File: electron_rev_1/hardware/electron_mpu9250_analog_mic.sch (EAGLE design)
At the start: 33 parts, among them IC2 S25FL128SAGNFI011, IC4 MIC_I2S_SPH0645, U1 MPU-9250, U2 Value, U3 OPA322AIDBVT

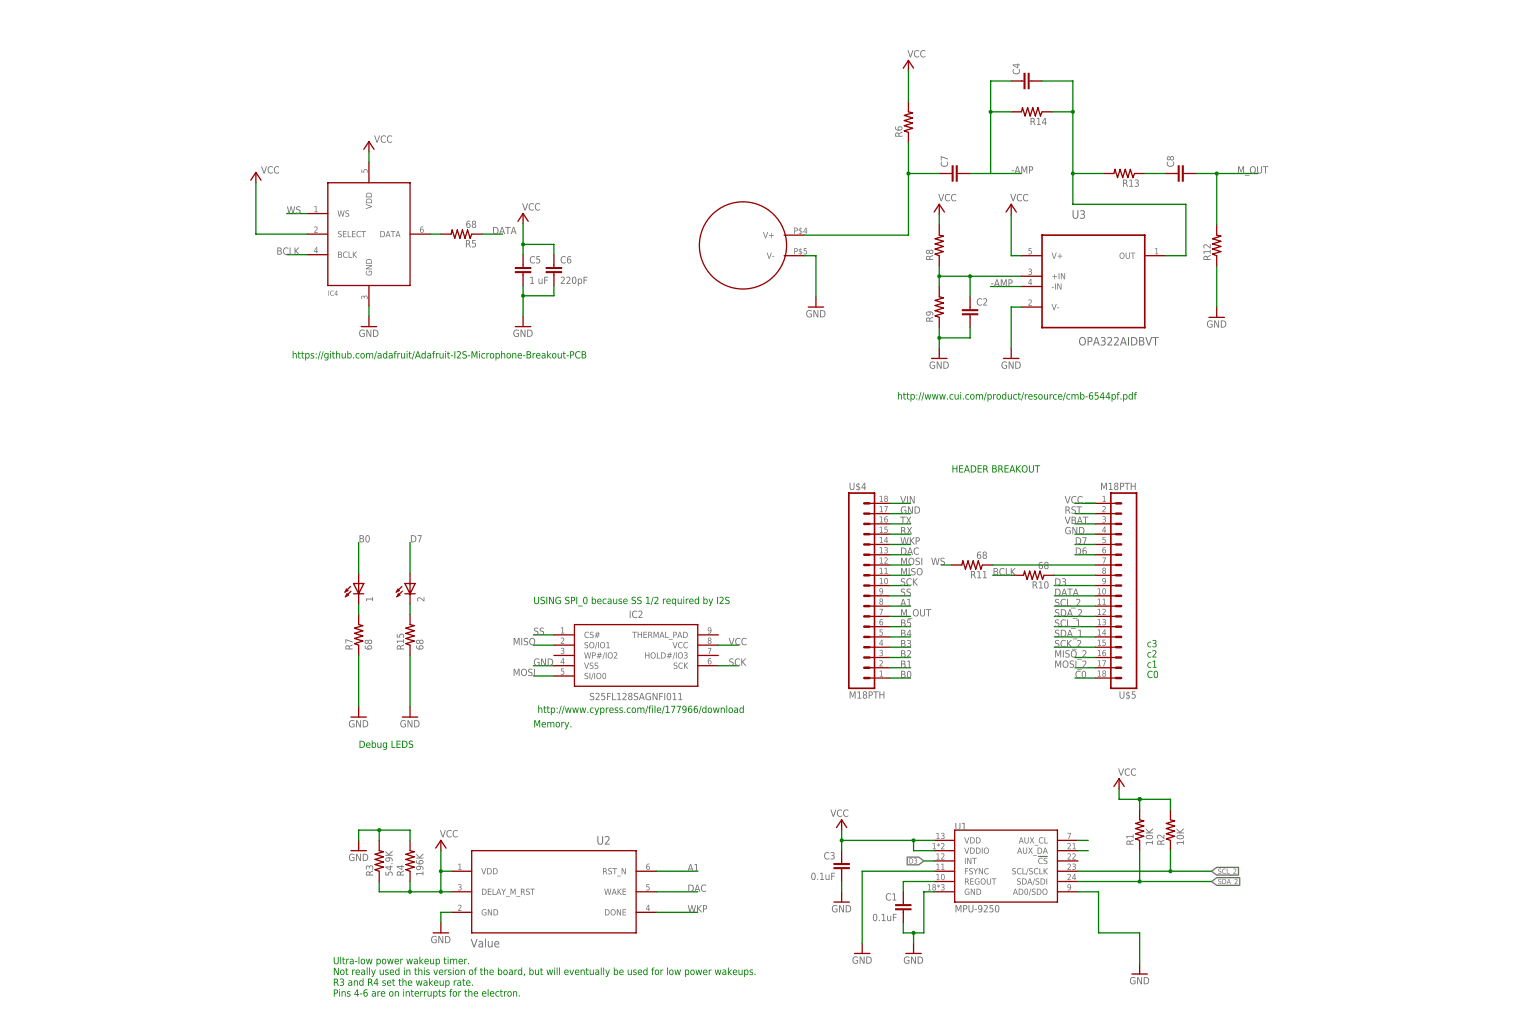
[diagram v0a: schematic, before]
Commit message: fixed grid issue in schematic. added sd card. added incomplete gas sensors
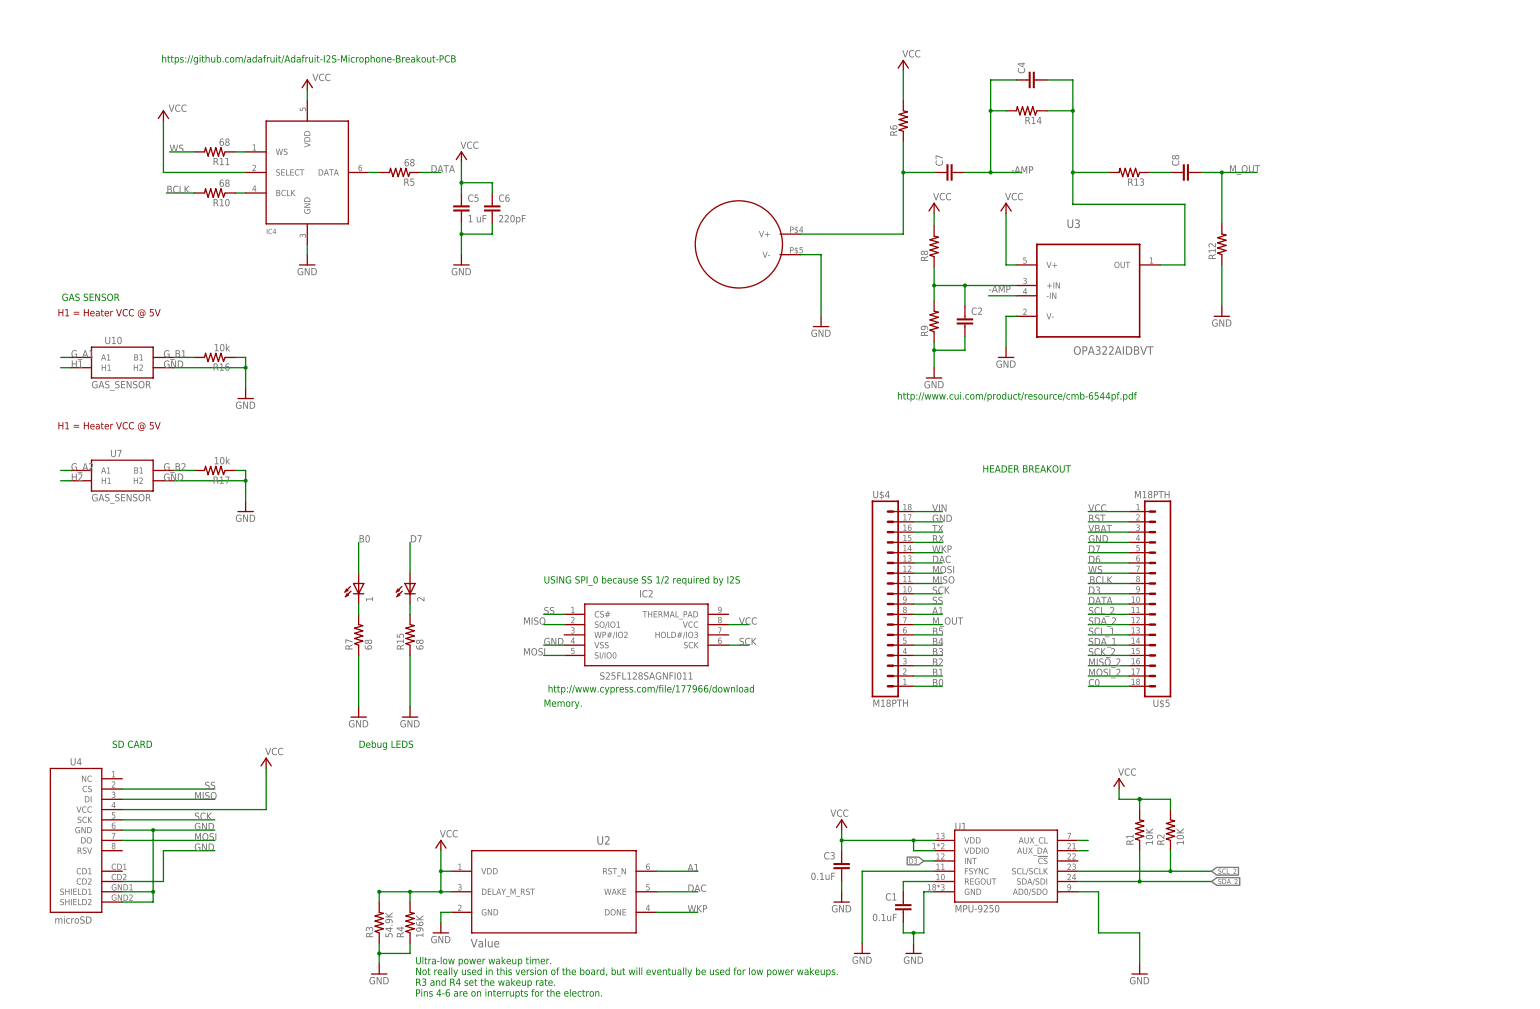
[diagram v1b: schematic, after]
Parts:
- added R16, R17: 10k, resistor:R-US_R0603
- added U10, U7: GAS_SENSOR, SparkFun:GAS_SENSOR
- added U4: microSD, SparkFun:USD-SOCKETSMD
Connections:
- new net G_A1: U10.A1
- new net G_A2: U7.A1
- new net G_B1: R16.2, U10.B1
- new net G_B2: R17.2, U7.B1
- new net H1: U10.H1
- new net H2: U7.H1
- net BCLK: now also U$5.8; no longer IC4.BCLK
- net GND: now also R16.1, R17.1, R3.1, R4.1, U10.H2, U4.CD2, U4.GND, U4.SHIELD1, U4.SHIELD2, U7.H2; no longer R3.2, R4.2
- net MISO: now also U4.DI
- net MOSI: now also U4.DO
- net N$2: now also IC4.WS, R11.1; no longer R10.1, U$5.8
- net N$4: now also IC4.BCLK, R10.1; no longer R11.1, U$5.7
- net SCK: now also U4.SCK
- net SS: now also U4.CS
- net VCC: now also R3.2, R4.2, U4.VCC; no longer R3.1, R4.1
- net WS: now also U$5.7; no longer IC4.WS
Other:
- note added: "GAS SENSOR"
- note added: "H1 = Heater VCC @ 5V"
- note added: "SD CARD"
- note removed: "C0"
- note removed: "c1"
- note removed: "c2"
- note removed: "c3"
- moved on the sheet: C2, C4, C5, C6, C7, C8, IC2, IC4, R10, R11, R12, R13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

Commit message: added in that good looking Cal logo... woooooo... also did a bit more wiring for the gas sensors
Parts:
- added L1: UCB_CAL100MIL, logos:UCB_CAL100MIL
- added SJ2: JUMPER_PAD-3-1&2_NC_BY_PASTE, SparkFun-Passives:JUMPER_PAD-3-1&2_NC_BY_PASTE
- added U5, U6: +12v, SparkFun-IC-Power:V_REG_78XX7812
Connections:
- new net N$10: SJ2.1, U5.IN, U6.IN
- net GND: now also SJ2.3, U5.GND, U6.GND
- net H1: now also U5.OUT
- net H2: now also U6.OUT
- net VCC: now also SJ2.2
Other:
- moved on the sheet: 1, 2, R15, R16, R17, R7, U10, U7

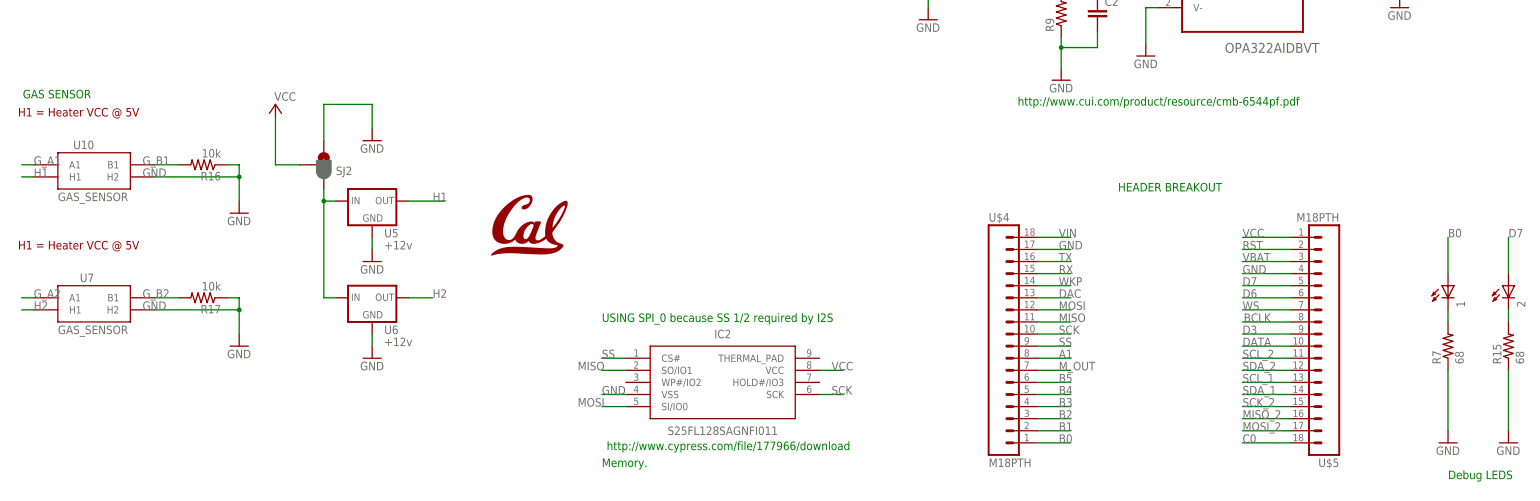
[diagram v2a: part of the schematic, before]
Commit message: generic gas sensors hooked up... haven't set up fancy CO relay thing yet. Don't know if it's worth it. Also last commit had gas sensors wired incorrectly
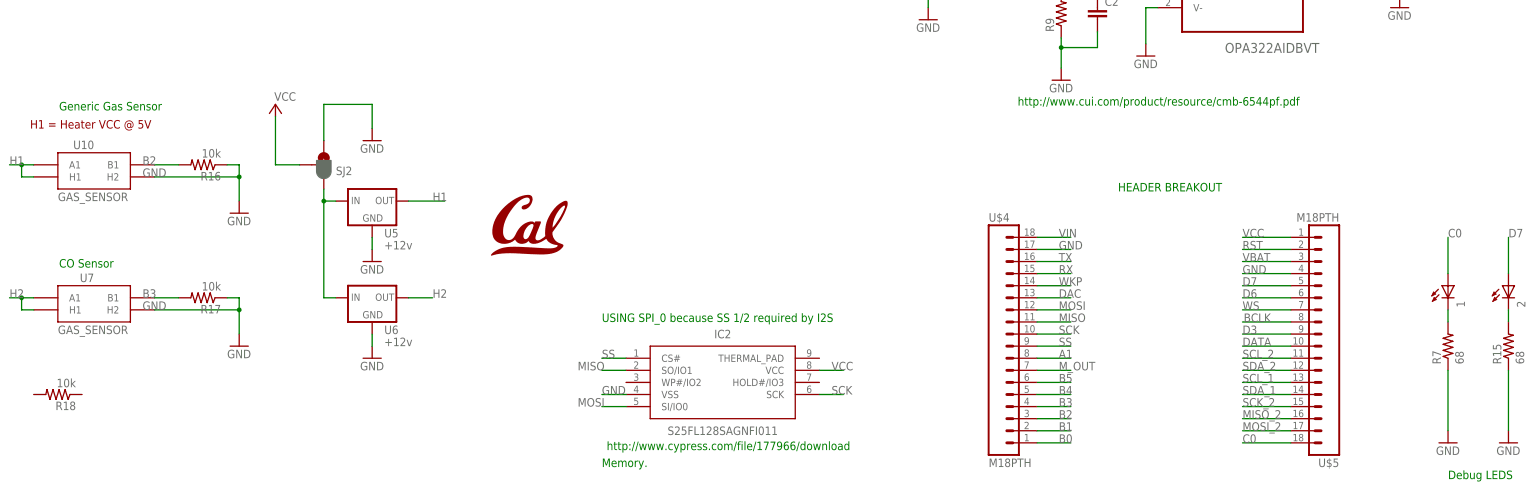
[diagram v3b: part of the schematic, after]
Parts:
- added R18: 10k, resistor:R-US_R0603
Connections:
- removed net G_A1: U10.A1
- removed net G_A2: U7.A1
- removed net G_B1: R16.2, U10.B1
- removed net G_B2: R17.2, U7.B1
- net B0: no longer 1.A
- net B2: now also R16.2, U10.B1
- net B3: now also R17.2, U7.B1
- net C0: now also 1.A
- net H1: now also U10.A1
- net H2: now also U7.A1
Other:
- note added: "CO Sensor"
- note added: "Generic Gas Sensor"
- note removed: "GAS SENSOR"
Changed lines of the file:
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@@
 <part name="GND19" library="supply1" library_urn="urn:adsk.eagle:library:371" deviceset="GND" device=""/>
 <part name="L1" library="logos" deviceset="UCB_CAL" device="100MIL"/>
+<part name="R18" library="resistor" library_urn="urn:adsk.eagle:library:348" deviceset="R-US_" device="R0603" package3d_urn="urn:adsk.eagle:package:26057/1" value="10k"/>
 </parts>
 <sheets>
@@
 <text x="33.02" y="45.72" size="1.778" layer="91">Memory. </text>
 <text x="141.478" y="103.632" size="1.778" layer="91">HEADER BREAKOUT</text>
-<text x="-88.646" y="123.19" size="1.778" layer="91">GAS SENSOR</text>
+<text x="-81.026" y="87.63" size="1.778" layer="91">CO Sensor</text>
 <text x="-73.66" y="35.56" size="1.778" layer="91">SD CARD</text>
 <text x="35.56" y="200.66" size="1.778" layer="91">SD CARD</text>
-<text x="-89.662" y="91.44" size="1.778" layer="94">H1 = Heater VCC @ 5V</text>
-<text x="-89.662" y="119.38" size="1.778" layer="94">H1 = Heater VCC @ 5V</text>
+<text x="-87.122" y="116.84" size="1.778" layer="94">H1 = Heater VCC @ 5V</text>
+<text x="-81.026" y="120.65" size="1.778" layer="91">Generic Gas Sensor</text>
 </plain>
 <instances>
@@
 <instance part="GND19" gate="1" x="-15.24" y="114.3"/>
 <instance part="L1" gate="G$1" x="17.78" y="96.52"/>
+<instance part="R18" gate="G$1" x="-81.28" y="60.96" rot="R180"/>
 </instances>
 <busses>
@@
 <label x="129.032" y="58.42" size="1.778" layer="95"/>
 </segment>
+<segment>
+<label x="-63.5" y="81.28" size="1.778" layer="95"/>
+<pinref part="U7" gate="G$1" pin="B1"/>
+<pinref part="R17" gate="G$1" pin="2"/>
+<wire x1="-60.96" y1="81.28" x2="-55.88" y2="81.28" width="0.1524" layer="91"/>
+</segment>
 </net>
 <net name="B2" class="0">
@@
 <label x="129.032" y="55.88" size="1.778" layer="95"/>
 </segment>
+<segment>
+<label x="-63.5" y="109.22" size="1.778" layer="95"/>
+<pinref part="U10" gate="G$1" pin="B1"/>
+<pinref part="R16" gate="G$1" pin="2"/>
+<wire x1="-60.96" y1="109.22" x2="-55.88" y2="109.22" width="0.1524" layer="91"/>
+</segment>
 </net>
 <net name="B1" class="0">
@@
 <label x="129.032" y="50.8" size="1.778" layer="95"/>
 </segment>
+</net>
+<net name="RST" class="0">
+<segment>
+<pinref part="U$5" gate="G$1" pin="2"/>
+<wire x1="177.8" y1="91.44" x2="167.64" y2="91.44" width="0.1524" layer="91"/>
+<label x="167.64" y="91.44" size="1.778" layer="95"/>
+</segment>
+</net>
+<net name="VBAT" class="0">
+<segment>
+<pinref part="U$5" gate="G$1" pin="3"/>
+<wire x1="177.8" y1="88.9" x2="167.64" y2="88.9" width="0.1524" layer="91"/>
+<label x="167.64" y="88.9" size="1.778" layer="95"/>
+</segment>
+</net>
+<net name="D7" class="0">
+<segment>
+<pinref part="U$5" gate="G$1" pin="5"/>
+<wire x1="177.8" y1="83.82" x2="167.64" y2="83.82" width="0.1524" layer="91"/>
+<label x="167.64" y="83.82" size="1.778" layer="95"/>
+</segment>
+<segment>
+<pinref part="2" gate="G$1" pin="A"/>
+<wire x1="223.52" y1="86.36" x2="223.52" y2="93.98" width="0.1524" layer="91"/>
+<label x="223.52" y="93.98" size="1.778" layer="95"/>
+</segment>
+</net>
+<net name="SS" class="0">
+<segment>
+<pinref part="IC2" gate="G$1" pin="CS#"/>
+<wire x1="38.1" y1="68.58" x2="33.02" y2="68.58" width="0.1524" layer="91"/>
+<label x="33.02" y="68.58" size="1.778" layer="95"/>
+</segment>
+<segment>
+<pinref part="U$4" gate="G$1" pin="9"/>
+<wire x1="124.46" y1="71.12" x2="131.572" y2="71.12" width="0.1524" layer="91"/>
+<label x="129.032" y="71.12" size="1.778" layer="95"/>
+</segment>
+<segment>
+<wire x1="-71.12" y1="25.4" x2="-48.26" y2="25.4" width="0.1524" layer="91"/>
+<pinref part="U4" gate="G$1" pin="CS"/>
+<label x="-50.8" y="25.4" size="1.778" layer="95"/>
+</segment>
+</net>
+<net name="MISO_2" class="0">
+<segment>
+<pinref part="U$5" gate="G$1" pin="16"/>
+<wire x1="177.8" y1="55.88" x2="167.64" y2="55.88" width="0.1524" layer="91"/>
+<label x="167.64" y="55.88" size="1.778" layer="95"/>
+</segment>
+</net>
+<net name="MOSI_2" class="0">
+<segment>
+<pinref part="U$5" gate="G$1" pin="17"/>
+<wire x1="177.8" y1="53.34" x2="167.64" y2="53.34" width="0.1524" layer="91"/>
+<label x="167.64" y="53.34" size="1.778" layer="95"/>
+</segment>
+</net>
+<net name="C0" class="0">
+<segment>
+<pinref part="U$5" gate="G$1" pin="18"/>
+<wire x1="177.8" y1="50.8" x2="167.64" y2="50.8" width="0.1524" layer="91"/>
+<label x="167.64" y="50.8" size="1.778" layer="95"/>
+</segment>
 <segment>
 <pinref part="1" gate="G$1" pin="A"/>
 <wire x1="210.82" y1="86.36" x2="210.82" y2="93.98" width="0.1524" layer="91"/>
 <label x="210.82" y="93.98" size="1.778" layer="95"/>
-</segment>
-</net>
-<net name="RST" class="0">
-<segment>
-<pinref part="U$5" gate="G$1" pin="2"/>
-<wire x1="177.8" y1="91.44" x2="167.64" y2="91.44" width="0.1524" layer="91"/>
-<label x="167.64" y="91.44" size="1.778" layer="95"/>
-</segment>
-</net>
-<net name="VBAT" class="0">
-<segment>
-<pinref part="U$5" gate="G$1" pin="3"/>
-<wire x1="177.8" y1="88.9" x2="167.64" y2="88.9" width="0.1524" layer="91"/>
-<label x="167.64" y="88.9" size="1.778" layer="95"/>
-</segment>
-</net>
-<net name="D7" class="0">
-<segment>
-<pinref part="U$5" gate="G$1" pin="5"/>
-<wire x1="177.8" y1="83.82" x2="167.64" y2="83.82" width="0.1524" layer="91"/>
-<label x="167.64" y="83.82" size="1.778" layer="95"/>
-</segment>
-<segment>
-<pinref part="2" gate="G$1" pin="A"/>
-<wire x1="223.52" y1="86.36" x2="223.52" y2="93.98" width="0.1524" layer="91"/>
-<label x="223.52" y="93.98" size="1.778" layer="95"/>
-</segment>
-</net>
-<net name="SS" class="0">
-<segment>
-<pinref part="IC2" gate="G$1" pin="CS#"/>
-<wire x1="38.1" y1="68.58" x2="33.02" y2="68.58" width="0.1524" layer="91"/>
-<label x="33.02" y="68.58" size="1.778" layer="95"/>
-</segment>
-<segment>
-<pinref part="U$4" gate="G$1" pin="9"/>
-<wire x1="124.46" y1="71.12" x2="131.572" y2="71.12" width="0.1524" layer="91"/>
-<label x="129.032" y="71.12" size="1.778" layer="95"/>
-</segment>
-<segment>
-<wire x1="-71.12" y1="25.4" x2="-48.26" y2="25.4" width="0.1524" layer="91"/>
-<pinref part="U4" gate="G$1" pin="CS"/>
-<label x="-50.8" y="25.4" size="1.778" layer="95"/>
-</segment>
-</net>
-<net name="MISO_2" class="0">
-<segment>
-<pinref part="U$5" gate="G$1" pin="16"/>
-<wire x1="177.8" y1="55.88" x2="167.64" y2="55.88" width="0.1524" layer="91"/>
-<label x="167.64" y="55.88" size="1.778" layer="95"/>
-</segment>
-</net>
-<net name="MOSI_2" class="0">
-<segment>
-<pinref part="U$5" gate="G$1" pin="17"/>
-<wire x1="177.8" y1="53.34" x2="167.64" y2="53.34" width="0.1524" layer="91"/>
-<label x="167.64" y="53.34" size="1.778" layer="95"/>
-</segment>
-</net>
-<net name="C0" class="0">
-<segment>
-<pinref part="U$5" gate="G$1" pin="18"/>
-<wire x1="177.8" y1="50.8" x2="167.64" y2="50.8" width="0.1524" layer="91"/>
-<label x="167.64" y="50.8" size="1.778" layer="95"/>
 </segment>
 </net>
@@
 <segment>
 <wire x1="-88.9" y1="106.68" x2="-86.36" y2="106.68" width="0.1524" layer="91"/>
-<label x="-86.36" y="106.68" size="1.778" layer="95"/>
 <pinref part="U10" gate="G$1" pin="H1"/>
+<wire x1="-88.9" y1="109.22" x2="-86.36" y2="109.22" width="0.1524" layer="91"/>
+<label x="-91.44" y="109.22" size="1.778" layer="95"/>
+<pinref part="U10" gate="G$1" pin="A1"/>
+<wire x1="-88.9" y1="106.68" x2="-88.9" y2="109.22" width="0.1524" layer="91"/>
+<wire x1="-88.9" y1="109.22" x2="-91.44" y2="109.22" width="0.1524" layer="91"/>
+<junction x="-88.9" y="109.22"/>
 </segment>
 <segment>
@@
 <segment>
 <wire x1="-88.9" y1="78.74" x2="-86.36" y2="78.74" width="0.1524" layer="91"/>
-<label x="-86.36" y="78.74" size="1.778" layer="95"/>
 <pinref part="U7" gate="G$1" pin="H1"/>
+<wire x1="-88.9" y1="81.28" x2="-86.36" y2="81.28" width="0.1524" layer="91"/>
+<label x="-91.44" y="81.28" size="1.778" layer="95"/>
+<pinref part="U7" gate="G$1" pin="A1"/>
+<wire x1="-88.9" y1="78.74" x2="-88.9" y2="81.28" width="0.1524" layer="91"/>
+<wire x1="-88.9" y1="81.28" x2="-91.44" y2="81.28" width="0.1524" layer="91"/>
+<junction x="-88.9" y="81.28"/>
 </segment>
 <segment>
@@
 </segment>
 </net>
-<net name="G_A2" class="0">
-<segment>
-<wire x1="-88.9" y1="81.28" x2="-86.36" y2="81.28" width="0.1524" layer="91"/>
-<label x="-86.36" y="81.28" size="1.778" layer="95"/>
-<pinref part="U7" gate="G$1" pin="A1"/>
-</segment>
-</net>
-<net name="G_B2" class="0">
-<segment>
-<label x="-63.5" y="81.28" size="1.778" layer="95"/>
-<pinref part="U7" gate="G$1" pin="B1"/>
-<pinref part="R17" gate="G$1" pin="2"/>
-<wire x1="-60.96" y1="81.28" x2="-55.88" y2="81.28" width="0.1524" layer="91"/>
-</segment>
-</net>
-<net name="G_B1" class="0">
-<segment>
-<label x="-63.5" y="109.22" size="1.778" layer="95"/>
-<pinref part="U10" gate="G$1" pin="B1"/>
-<pinref part="R16" gate="G$1" pin="2"/>
-<wire x1="-60.96" y1="109.22" x2="-55.88" y2="109.22" width="0.1524" layer="91"/>
-</segment>
-</net>
-<net name="G_A1" class="0">
-<segment>
-<wire x1="-88.9" y1="109.22" x2="-86.36" y2="109.22" width="0.1524" layer="91"/>
-<label x="-86.36" y="109.22" size="1.778" layer="95"/>
-<pinref part="U10" gate="G$1" pin="A1"/>
-</segment>
-</net>
